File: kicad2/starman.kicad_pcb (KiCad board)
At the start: 2 copper layers, 160 x 150 mm, 156 parts, among them J1 Barrel_Jack, P1 USB_C_Plug_USB2.0, U1 ESP32-S2-MINI-1, U2 PCA9959, U3 PCA9959, U4 PCA9959, U5 PCA9959, U6 LF33_TO220, U7 LF50_TO220, U8 PCA9959, U9 PCA9959

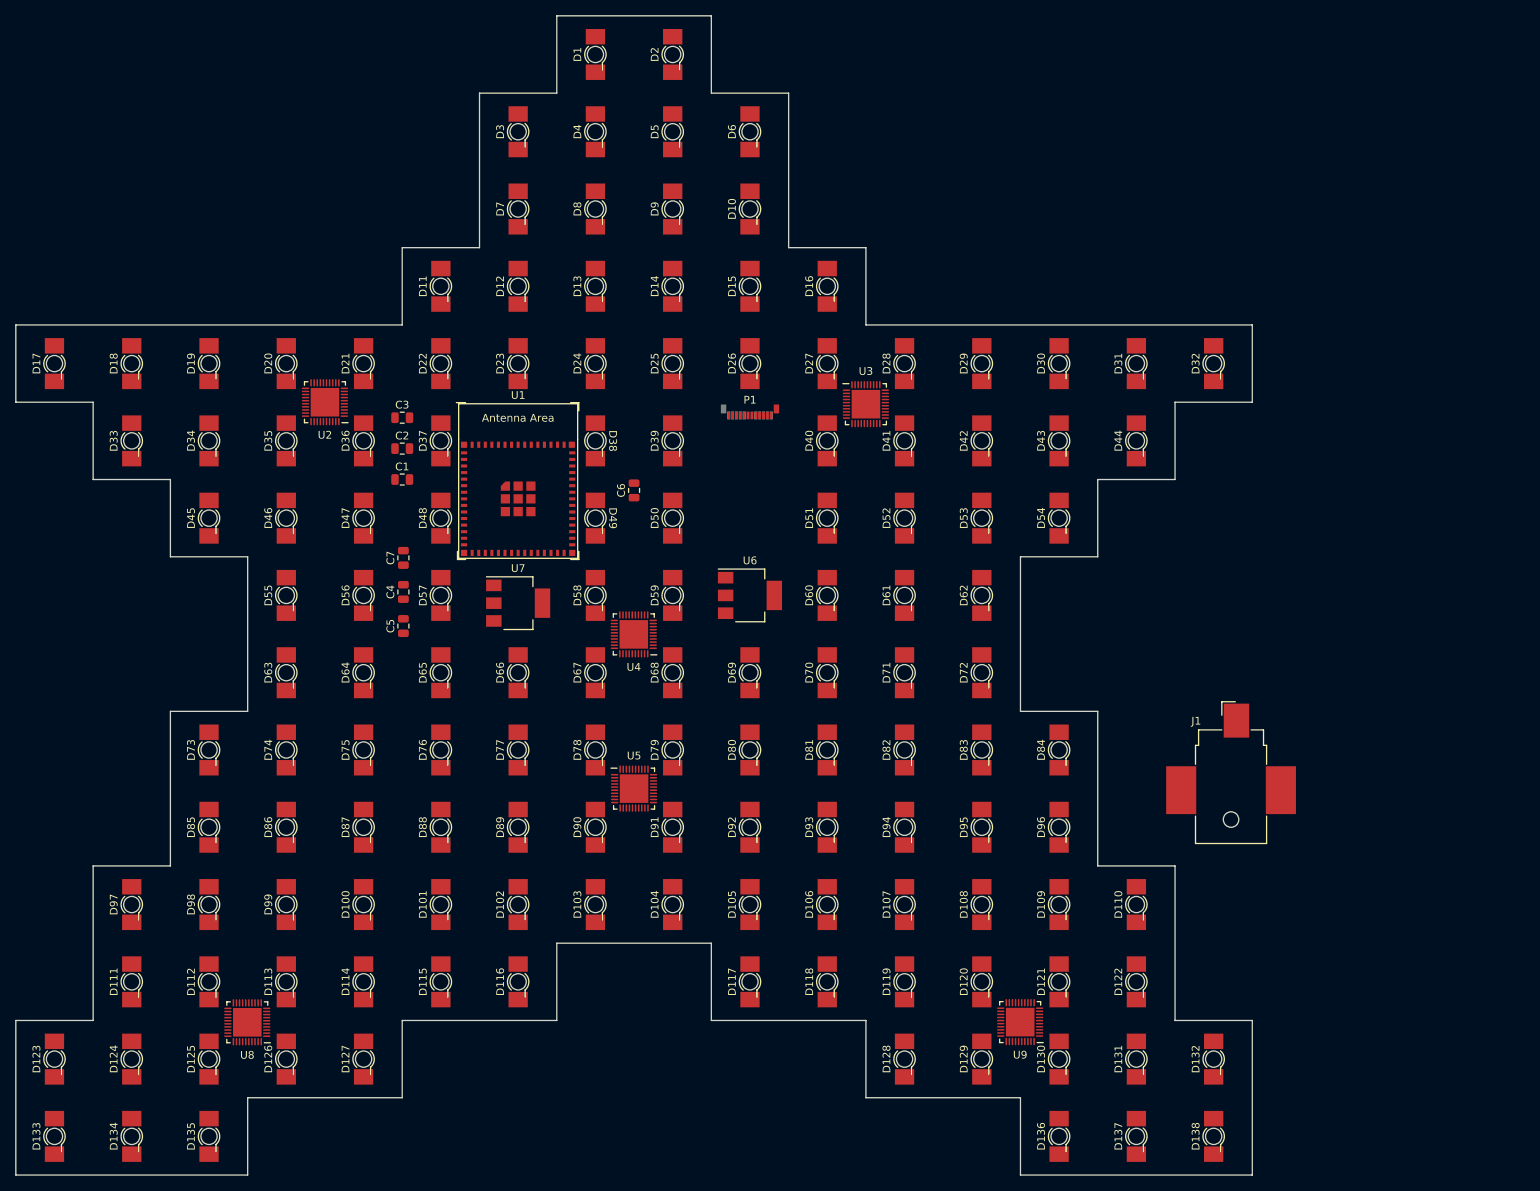
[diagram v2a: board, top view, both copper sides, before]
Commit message: Route U2 and U3 LEDs
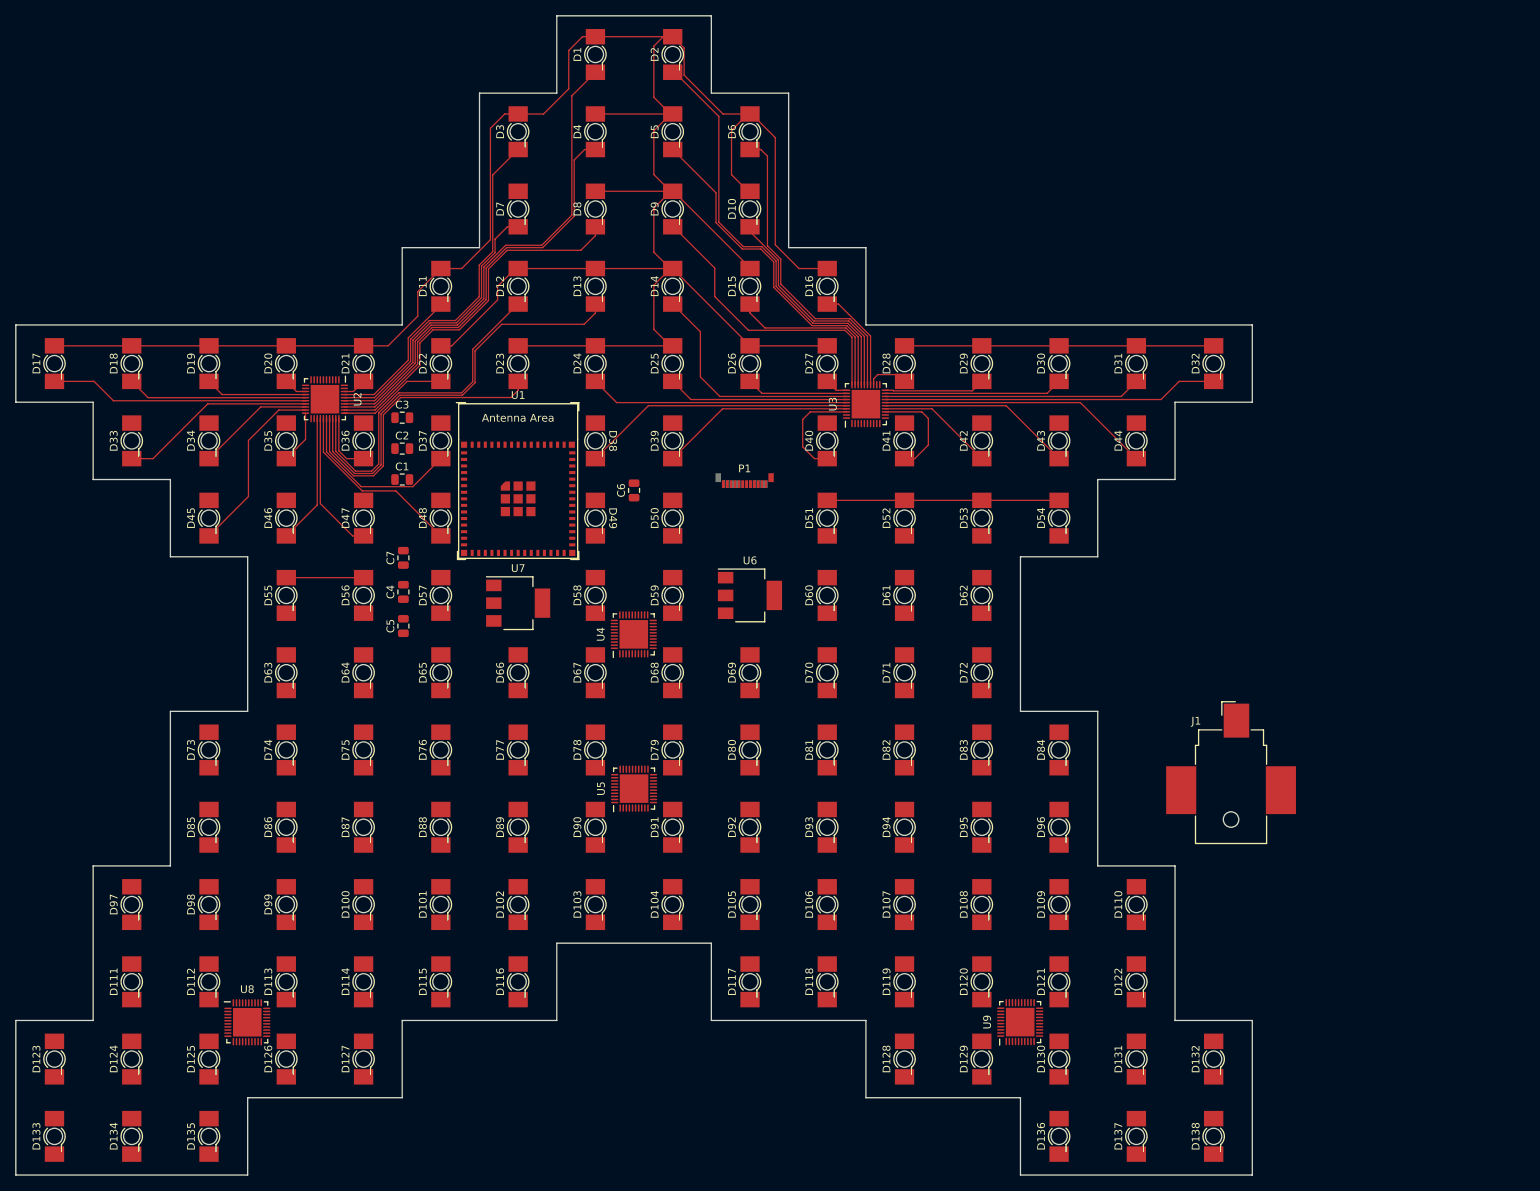
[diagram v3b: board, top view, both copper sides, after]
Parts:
- moved P1 8.92 mm to (124.3, 90.6)
- moved U2 0.39 mm to (70.0, 79.6), turned to 270 degrees
- turned U3 to 90 degrees
- turned U4 to 90 degrees
- turned U5 to 90 degrees
- turned U8 to 0 degrees
- turned U9 to 90 degrees
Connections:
- D1 pad 2: Net-(D1-Pad2) -> (no net)
- D10 pad 2: Net-(D10-Pad2) -> (no net)
- D100 pad 2: Net-(D100-Pad2) -> (no net)
- D101 pad 2: Net-(D101-Pad2) -> (no net)
- D102 pad 2: Net-(D102-Pad2) -> (no net)
- D103 pad 2: Net-(D103-Pad2) -> (no net)
- D104 pad 2: Net-(D104-Pad2) -> (no net)
- D105 pad 2: Net-(D105-Pad2) -> (no net)
- D106 pad 2: Net-(D106-Pad2) -> (no net)
- D107 pad 2: Net-(D107-Pad2) -> (no net)
- D108 pad 2: Net-(D108-Pad2) -> (no net)
- D109 pad 2: Net-(D109-Pad2) -> (no net)
- D11 pad 2: Net-(D11-Pad2) -> (no net)
- D110 pad 2: Net-(D110-Pad2) -> (no net)
- D111 pad 2: Net-(D111-Pad2) -> (no net)
- D112 pad 2: Net-(D112-Pad2) -> (no net)
- D113 pad 2: Net-(D113-Pad2) -> (no net)
- D114 pad 2: Net-(D114-Pad2) -> (no net)
- D115 pad 2: Net-(D115-Pad2) -> (no net)
- D116 pad 2: Net-(D116-Pad2) -> (no net)
- D117 pad 2: Net-(D117-Pad2) -> (no net)
- D118 pad 2: Net-(D118-Pad2) -> (no net)
- D119 pad 2: Net-(D119-Pad2) -> (no net)
- D12 pad 2: Net-(D12-Pad2) -> (no net)
- D120 pad 2: Net-(D120-Pad2) -> (no net)
- D121 pad 2: Net-(D121-Pad2) -> (no net)
- D122 pad 2: Net-(D122-Pad2) -> (no net)
- D123 pad 2: Net-(D123-Pad2) -> (no net)
- D124 pad 2: Net-(D124-Pad2) -> (no net)
- D125 pad 2: Net-(D125-Pad2) -> (no net)
- D126 pad 2: Net-(D126-Pad2) -> (no net)
- D127 pad 2: Net-(D127-Pad2) -> (no net)
- D128 pad 2: Net-(D128-Pad2) -> (no net)
- D129 pad 2: Net-(D129-Pad2) -> (no net)
- D13 pad 2: Net-(D13-Pad2) -> (no net)
- D130 pad 2: Net-(D130-Pad2) -> (no net)
- D131 pad 2: Net-(D131-Pad2) -> (no net)
- D132 pad 2: Net-(D132-Pad2) -> (no net)
- D133 pad 2: Net-(D133-Pad2) -> (no net)
- D134 pad 2: Net-(D134-Pad2) -> (no net)
- D135 pad 2: Net-(D135-Pad2) -> (no net)
- D136 pad 2: Net-(D136-Pad2) -> (no net)
- D137 pad 2: Net-(D137-Pad2) -> (no net)
- D138 pad 2: Net-(D138-Pad2) -> (no net)
- D14 pad 2: Net-(D14-Pad2) -> (no net)
- D15 pad 2: Net-(D15-Pad2) -> (no net)
- D16 pad 2: Net-(D16-Pad2) -> (no net)
- D17 pad 2: Net-(D17-Pad2) -> (no net)
- D18 pad 2: Net-(D18-Pad2) -> (no net)
- D19 pad 2: Net-(D19-Pad2) -> (no net)
- D2 pad 2: Net-(D2-Pad2) -> (no net)
- D20 pad 2: Net-(D20-Pad2) -> (no net)
- D21 pad 2: Net-(D21-Pad2) -> (no net)
- D22 pad 2: Net-(D22-Pad2) -> (no net)
- D23 pad 2: Net-(D23-Pad2) -> (no net)
- D24 pad 2: Net-(D24-Pad2) -> (no net)
- D25 pad 2: Net-(D25-Pad2) -> (no net)
- D26 pad 2: Net-(D26-Pad2) -> (no net)
- D27 pad 2: Net-(D27-Pad2) -> (no net)
- D28 pad 2: Net-(D28-Pad2) -> (no net)
- D29 pad 2: Net-(D29-Pad2) -> (no net)
- D3 pad 2: Net-(D3-Pad2) -> (no net)
- D30 pad 2: Net-(D30-Pad2) -> (no net)
- D31 pad 2: Net-(D31-Pad2) -> (no net)
- D32 pad 2: Net-(D32-Pad2) -> (no net)
- D33 pad 2: Net-(D33-Pad2) -> (no net)
- D34 pad 2: Net-(D34-Pad2) -> (no net)
- D35 pad 2: Net-(D35-Pad2) -> (no net)
- D36 pad 2: Net-(D36-Pad2) -> (no net)
- D37 pad 2: Net-(D37-Pad2) -> (no net)
- D38 pad 2: Net-(D38-Pad2) -> (no net)
- D39 pad 2: Net-(D39-Pad2) -> (no net)
- D4 pad 2: Net-(D4-Pad2) -> (no net)
- D40 pad 2: Net-(D40-Pad2) -> (no net)
- D41 pad 2: Net-(D41-Pad2) -> (no net)
- D42 pad 2: Net-(D42-Pad2) -> (no net)
- D43 pad 2: Net-(D43-Pad2) -> (no net)
- D44 pad 2: Net-(D44-Pad2) -> (no net)
- D45 pad 2: Net-(D45-Pad2) -> (no net)
- D46 pad 2: Net-(D46-Pad2) -> (no net)
- D47 pad 2: Net-(D47-Pad2) -> (no net)
- D48 pad 2: Net-(D48-Pad2) -> (no net)
- D49 pad 2: Net-(D49-Pad2) -> (no net)
- D5 pad 2: Net-(D5-Pad2) -> (no net)
- D50 pad 2: Net-(D50-Pad2) -> (no net)
- D51 pad 2: Net-(D51-Pad2) -> (no net)
- D52 pad 2: Net-(D52-Pad2) -> (no net)
- D53 pad 2: Net-(D53-Pad2) -> (no net)
- D54 pad 2: Net-(D54-Pad2) -> (no net)
- D55 pad 2: Net-(D55-Pad2) -> (no net)
- D56 pad 2: Net-(D56-Pad2) -> (no net)
- D57 pad 2: Net-(D57-Pad2) -> (no net)
- D58 pad 2: Net-(D58-Pad2) -> (no net)
- D59 pad 2: Net-(D59-Pad2) -> (no net)
- D6 pad 2: Net-(D6-Pad2) -> (no net)
- D60 pad 2: Net-(D60-Pad2) -> (no net)
- D61 pad 2: Net-(D61-Pad2) -> (no net)
- D62 pad 2: Net-(D62-Pad2) -> (no net)
- D63 pad 2: Net-(D63-Pad2) -> (no net)
- D64 pad 2: Net-(D64-Pad2) -> (no net)
- D65 pad 2: Net-(D65-Pad2) -> (no net)
- D66 pad 2: Net-(D66-Pad2) -> (no net)
- D67 pad 2: Net-(D67-Pad2) -> (no net)
- D68 pad 2: Net-(D68-Pad2) -> (no net)
- D69 pad 2: Net-(D69-Pad2) -> (no net)
- D7 pad 2: Net-(D7-Pad2) -> (no net)
- D70 pad 2: Net-(D70-Pad2) -> (no net)
- D71 pad 2: Net-(D71-Pad2) -> (no net)
- D72 pad 2: Net-(D72-Pad2) -> (no net)
- D73 pad 1: Net-(D73-Pad1) -> (no net)
- D73 pad 2: Net-(D73-Pad2) -> (no net)
- D74 pad 2: Net-(D74-Pad2) -> (no net)
- D75 pad 2: Net-(D75-Pad2) -> (no net)
- D76 pad 2: Net-(D76-Pad2) -> (no net)
- D77 pad 2: Net-(D77-Pad2) -> (no net)
- D78 pad 2: Net-(D78-Pad2) -> (no net)
- D79 pad 2: Net-(D79-Pad2) -> (no net)
- D8 pad 2: Net-(D8-Pad2) -> (no net)
- D80 pad 2: Net-(D80-Pad2) -> (no net)
- D81 pad 2: Net-(D81-Pad2) -> (no net)
- D82 pad 2: Net-(D82-Pad2) -> (no net)
- D83 pad 2: Net-(D83-Pad2) -> (no net)
- D84 pad 2: Net-(D84-Pad2) -> (no net)
- D85 pad 2: Net-(D85-Pad2) -> (no net)
- D86 pad 2: Net-(D86-Pad2) -> (no net)
- D87 pad 2: Net-(D87-Pad2) -> (no net)
- D88 pad 2: Net-(D88-Pad2) -> (no net)
- D89 pad 2: Net-(D89-Pad2) -> (no net)
- D9 pad 2: Net-(D9-Pad2) -> (no net)
- D90 pad 2: Net-(D90-Pad2) -> (no net)
- D91 pad 2: Net-(D91-Pad2) -> (no net)
- D92 pad 2: Net-(D92-Pad2) -> (no net)
- D93 pad 2: Net-(D93-Pad2) -> (no net)
- D94 pad 2: Net-(D94-Pad2) -> (no net)
- D95 pad 2: Net-(D95-Pad2) -> (no net)
- D96 pad 2: Net-(D96-Pad2) -> (no net)
- D97 pad 2: Net-(D97-Pad2) -> (no net)
- D98 pad 2: Net-(D98-Pad2) -> (no net)
- D99 pad 2: Net-(D99-Pad2) -> (no net)
- P1 pad A5: Net-(P1-PadA5) -> (no net)
- P1 pad A8: Net-(P1-PadA8) -> (no net)
- P1 pad B5: Net-(P1-PadB5) -> (no net)
- P1 pad B8: Net-(P1-PadB8) -> (no net)
- U1 pad 10: Net-(U1-Pad10) -> (no net)
- U1 pad 11: Net-(U1-Pad11) -> (no net)
- U1 pad 12: Net-(U1-Pad12) -> (no net)
- U1 pad 13: Net-(U1-Pad13) -> (no net)
- U1 pad 14: Net-(U1-Pad14) -> (no net)
- U1 pad 15: Net-(U1-Pad15) -> (no net)
- U1 pad 16: Net-(U1-Pad16) -> (no net)
- U1 pad 17: Net-(U1-Pad17) -> (no net)
- U1 pad 18: Net-(U1-Pad18) -> (no net)
- U1 pad 19: Net-(U1-Pad19) -> (no net)
- U1 pad 20: Net-(U1-Pad20) -> (no net)
- U1 pad 21: Net-(U1-Pad21) -> (no net)
- U1 pad 22: Net-(U1-Pad22) -> (no net)
- U1 pad 25: Net-(U1-Pad25) -> (no net)
- U1 pad 26: Net-(U1-Pad26) -> (no net)
- U1 pad 27: Net-(U1-Pad27) -> (no net)
- U1 pad 28: Net-(U1-Pad28) -> (no net)
- U1 pad 29: Net-(U1-Pad29) -> (no net)
- U1 pad 31: Net-(U1-Pad31) -> (no net)
- U1 pad 32: Net-(U1-Pad32) -> (no net)
- U1 pad 33: Net-(U1-Pad33) -> (no net)
- U1 pad 34: Net-(U1-Pad34) -> (no net)
- U1 pad 35: Net-(U1-Pad35) -> (no net)
- U1 pad 36: Net-(U1-Pad36) -> (no net)
- U1 pad 37: Net-(U1-Pad37) -> (no net)
- U1 pad 38: Net-(U1-Pad38) -> (no net)
- U1 pad 39: Net-(U1-Pad39) -> (no net)
- U1 pad 4: /BOOT -> (no net)
- U1 pad 40: Net-(U1-Pad40) -> (no net)
- U1 pad 41: Net-(U1-Pad41) -> (no net)
- U1 pad 44: Net-(U1-Pad44) -> (no net)
- U1 pad 45: /RESET -> (no net)
- U1 pad 5: /IREF -> (no net)
- U1 pad 6: /BLANK -> (no net)
- U1 pad 7: /XLAT -> (no net)
- U1 pad 8: /SCLK -> (no net)
- U1 pad 9: /SIN -> (no net)
- U2 pad 1: Net-(U2-Pad1) -> (no net)
- U2 pad 10: Net-(U2-Pad10) -> (no net)
- U2 pad 11: Net-(U2-Pad11) -> (no net)
- U2 pad 12: Net-(U2-Pad12) -> (no net)
- U2 pad 13: Net-(D1-Pad1) -> Net-(D20-Pad1)
- U2 pad 14: Net-(D3-Pad1) -> Net-(D19-Pad1)
- U2 pad 15: Net-(D4-Pad1) -> Net-(D18-Pad1)
- U2 pad 16: Net-(D7-Pad1) -> Net-(D17-Pad1)
- U2 pad 17: Net-(D8-Pad1) -> Net-(D33-Pad1)
- U2 pad 18: Net-(D11-Pad1) -> Net-(D34-Pad1)
- U2 pad 19: Net-(D12-Pad1) -> Net-(D45-Pad1)
- U2 pad 2: Net-(U2-Pad2) -> (no net)
- U2 pad 20: Net-(D13-Pad1) -> Net-(D35-Pad1)
- U2 pad 21: Net-(U2-Pad21) -> (no net)
- U2 pad 22: Net-(U2-Pad22) -> (no net)
- U2 pad 23: Net-(D17-Pad1) -> Net-(D46-Pad1)
- U2 pad 24: Net-(D18-Pad1) -> Net-(D47-Pad1)
- U2 pad 25: Net-(D19-Pad1) -> Net-(D48-Pad1)
- U2 pad 26: Net-(D20-Pad1) -> Net-(D37-Pad1)
- U2 pad 27: Net-(D21-Pad1) -> Net-(D23-Pad1)
- U2 pad 28: Net-(D22-Pad1) -> Net-(D13-Pad1)
- U2 pad 29: Net-(D23-Pad1) -> Net-(D12-Pad1)
- U2 pad 3: Net-(U2-Pad3) -> (no net)
- U2 pad 30: Net-(D33-Pad1) -> Net-(D36-Pad1)
- U2 pad 31: Net-(D34-Pad1) -> Net-(D22-Pad1)
- U2 pad 32: Net-(D35-Pad1) -> Net-(D8-Pad1)
- U2 pad 33: Net-(D36-Pad1) -> Net-(D4-Pad1)
- U2 pad 34: Net-(D37-Pad1) -> Net-(D1-Pad1)
- U2 pad 35: Net-(D45-Pad1) -> Net-(D7-Pad1)
- U2 pad 36: Net-(D46-Pad1) -> Net-(D3-Pad1)
- U2 pad 37: Net-(D47-Pad1) -> Net-(D11-Pad1)
- U2 pad 38: Net-(D48-Pad1) -> Net-(D21-Pad1)
- U2 pad 39: Net-(U2-Pad39) -> (no net)
- U2 pad 4: Net-(U2-Pad4) -> (no net)
- U2 pad 40: Net-(U2-Pad40) -> (no net)
- U2 pad 5: Net-(U2-Pad5) -> (no net)
- U2 pad 6: Net-(U2-Pad6) -> (no net)
- U2 pad 7: Net-(U2-Pad7) -> (no net)
- U2 pad 8: Net-(U2-Pad8) -> (no net)
- U2 pad 9: Net-(U2-Pad9) -> (no net)
- U3 pad 1: Net-(U3-Pad1) -> (no net)
- U3 pad 10: Net-(U3-Pad10) -> (no net)
- U3 pad 11: Net-(U3-Pad11) -> (no net)
- U3 pad 12: Net-(U3-Pad12) -> (no net)
- U3 pad 13: Net-(D2-Pad1) -> Net-(D41-Pad1)
- U3 pad 14: Net-(D5-Pad1) -> Net-(D42-Pad1)
- U3 pad 15: Net-(D6-Pad1) -> Net-(D43-Pad1)
- U3 pad 16: Net-(D9-Pad1) -> Net-(D44-Pad1)
- U3 pad 17: Net-(D10-Pad1) -> Net-(D32-Pad1)
- U3 pad 18: Net-(D14-Pad1) -> Net-(D31-Pad1)
- U3 pad 19: Net-(D15-Pad1) -> Net-(D30-Pad1)
- U3 pad 2: Net-(U3-Pad2) -> (no net)
- U3 pad 20: Net-(D16-Pad1) -> Net-(D29-Pad1)
- U3 pad 21: Net-(U3-Pad21) -> (no net)
- U3 pad 22: Net-(U3-Pad22) -> (no net)
- U3 pad 23: Net-(D24-Pad1) -> Net-(D28-Pad1)
- U3 pad 24: Net-(D25-Pad1) -> Net-(D16-Pad1)
- U3 pad 25: Net-(D26-Pad1) -> Net-(D6-Pad1)
- U3 pad 26: Net-(D27-Pad1) -> Net-(D10-Pad1)
- U3 pad 27: Net-(D28-Pad1) -> Net-(D2-Pad1)
- U3 pad 28: Net-(D29-Pad1) -> Net-(D5-Pad1)
- U3 pad 29: Net-(D30-Pad1) -> Net-(D15-Pad1)
- U3 pad 3: Net-(U3-Pad3) -> (no net)
- U3 pad 30: Net-(D31-Pad1) -> Net-(D9-Pad1)
- U3 pad 31: Net-(D32-Pad1) -> Net-(D27-Pad1)
- U3 pad 32: Net-(D38-Pad1) -> Net-(D26-Pad1)
- U3 pad 33: Net-(D39-Pad1) -> Net-(D14-Pad1)
- U3 pad 34: Net-(D40-Pad1) -> Net-(D25-Pad1)
- U3 pad 35: Net-(D41-Pad1) -> Net-(D24-Pad1)
- U3 pad 36: Net-(D42-Pad1) -> Net-(D38-Pad1)
- U3 pad 37: Net-(D43-Pad1) -> Net-(D39-Pad1)
- U3 pad 38: Net-(D44-Pad1) -> Net-(D40-Pad1)
- U3 pad 39: Net-(U3-Pad39) -> (no net)
- U3 pad 4: Net-(U3-Pad4) -> (no net)
- U3 pad 40: Net-(U3-Pad40) -> (no net)
- U3 pad 5: Net-(U3-Pad5) -> (no net)
- U3 pad 6: Net-(U3-Pad6) -> (no net)
- U3 pad 7: Net-(U3-Pad7) -> (no net)
- U3 pad 8: Net-(U3-Pad8) -> (no net)
- U3 pad 9: Net-(U3-Pad9) -> (no net)
- U4 pad 1: Net-(U4-Pad1) -> (no net)
- U4 pad 10: Net-(U4-Pad10) -> (no net)
- U4 pad 11: Net-(U4-Pad11) -> (no net)
- U4 pad 12: Net-(U4-Pad12) -> (no net)
- U4 pad 2: Net-(U4-Pad2) -> (no net)
- U4 pad 21: Net-(U4-Pad21) -> (no net)
- U4 pad 22: Net-(U4-Pad22) -> (no net)
- U4 pad 3: Net-(U4-Pad3) -> (no net)
- U4 pad 39: Net-(U4-Pad39) -> (no net)
- U4 pad 4: Net-(U4-Pad4) -> (no net)
- U4 pad 40: Net-(U4-Pad40) -> (no net)
- U4 pad 5: Net-(U4-Pad5) -> (no net)
- U4 pad 6: Net-(U4-Pad6) -> (no net)
- U4 pad 7: Net-(U4-Pad7) -> (no net)
- U4 pad 8: Net-(U4-Pad8) -> (no net)
- U4 pad 9: Net-(U4-Pad9) -> (no net)
- U5 pad 1: Net-(U5-Pad1) -> (no net)
- U5 pad 10: Net-(U5-Pad10) -> (no net)
- U5 pad 11: Net-(U5-Pad11) -> (no net)
- U5 pad 12: Net-(U5-Pad12) -> (no net)
- U5 pad 13: Net-(D73-Pad1) -> (no net)
- U5 pad 14: Net-(D74-Pad1) -> Net-(D96-Pad1)
- U5 pad 15: Net-(D75-Pad1) -> Net-(D95-Pad1)
- U5 pad 16: Net-(D76-Pad1) -> Net-(D94-Pad1)
- U5 pad 17: Net-(D77-Pad1) -> Net-(D93-Pad1)
- U5 pad 18: Net-(D78-Pad1) -> Net-(D92-Pad1)
- U5 pad 19: Net-(D79-Pad1) -> Net-(D91-Pad1)
- U5 pad 2: Net-(U5-Pad2) -> (no net)
- U5 pad 20: Net-(D80-Pad1) -> Net-(D90-Pad1)
- U5 pad 21: Net-(U5-Pad21) -> (no net)
- U5 pad 22: Net-(U5-Pad22) -> (no net)
- U5 pad 23: Net-(D81-Pad1) -> Net-(D89-Pad1)
- U5 pad 24: Net-(D82-Pad1) -> Net-(D88-Pad1)
- U5 pad 25: Net-(D83-Pad1) -> Net-(D87-Pad1)
- U5 pad 26: Net-(D84-Pad1) -> Net-(D86-Pad1)
- U5 pad 28: Net-(D86-Pad1) -> Net-(D84-Pad1)
- U5 pad 29: Net-(D87-Pad1) -> Net-(D83-Pad1)
- U5 pad 3: Net-(U5-Pad3) -> (no net)
- U5 pad 30: Net-(D88-Pad1) -> Net-(D82-Pad1)
- U5 pad 31: Net-(D89-Pad1) -> Net-(D81-Pad1)
- U5 pad 32: Net-(D90-Pad1) -> Net-(D80-Pad1)
- U5 pad 33: Net-(D91-Pad1) -> Net-(D79-Pad1)
- U5 pad 34: Net-(D92-Pad1) -> Net-(D78-Pad1)
- U5 pad 35: Net-(D93-Pad1) -> Net-(D77-Pad1)
- U5 pad 36: Net-(D94-Pad1) -> Net-(D76-Pad1)
- U5 pad 37: Net-(D95-Pad1) -> Net-(D75-Pad1)
- U5 pad 38: Net-(D96-Pad1) -> Net-(D74-Pad1)
- U5 pad 39: Net-(U5-Pad39) -> (no net)
- U5 pad 4: Net-(U5-Pad4) -> (no net)
- U5 pad 40: Net-(U5-Pad40) -> (no net)
- U5 pad 5: Net-(U5-Pad5) -> (no net)
- U5 pad 6: Net-(U5-Pad6) -> (no net)
- U5 pad 7: Net-(U5-Pad7) -> (no net)
- U5 pad 8: Net-(U5-Pad8) -> (no net)
- U5 pad 9: Net-(U5-Pad9) -> (no net)
- U8 pad 1: Net-(U8-Pad1) -> (no net)
- U8 pad 10: Net-(U8-Pad10) -> (no net)
- U8 pad 11: Net-(U8-Pad11) -> (no net)
- U8 pad 12: Net-(U8-Pad12) -> (no net)
- U8 pad 2: Net-(U8-Pad2) -> (no net)
- U8 pad 21: Net-(U8-Pad21) -> (no net)
- U8 pad 22: Net-(U8-Pad22) -> (no net)
- U8 pad 3: Net-(U8-Pad3) -> (no net)
- U8 pad 36: Net-(U8-Pad36) -> (no net)
- U8 pad 37: Net-(U8-Pad37) -> (no net)
- U8 pad 38: Net-(U8-Pad38) -> (no net)
- U8 pad 39: Net-(U8-Pad39) -> (no net)
- U8 pad 4: Net-(U8-Pad4) -> (no net)
- U8 pad 40: Net-(U8-Pad40) -> (no net)
- U8 pad 5: Net-(U8-Pad5) -> (no net)
- U8 pad 6: Net-(U8-Pad6) -> (no net)
- U8 pad 7: Net-(U8-Pad7) -> (no net)
- U8 pad 8: Net-(U8-Pad8) -> (no net)
- U8 pad 9: Net-(U8-Pad9) -> (no net)
- U9 pad 1: Net-(U9-Pad1) -> (no net)
- U9 pad 10: Net-(U9-Pad10) -> (no net)
- U9 pad 11: Net-(U9-Pad11) -> (no net)
- U9 pad 12: Net-(U9-Pad12) -> (no net)
- U9 pad 2: Net-(U9-Pad2) -> (no net)
- U9 pad 21: Net-(U9-Pad21) -> (no net)
- U9 pad 22: Net-(U9-Pad22) -> (no net)
- U9 pad 3: Net-(U9-Pad3) -> (no net)
- U9 pad 36: Net-(U9-Pad36) -> (no net)
- U9 pad 37: Net-(U9-Pad37) -> (no net)
- U9 pad 38: Net-(U9-Pad38) -> (no net)
- U9 pad 39: Net-(U9-Pad39) -> (no net)
- U9 pad 4: Net-(U9-Pad4) -> (no net)
- U9 pad 40: Net-(U9-Pad40) -> (no net)
- U9 pad 5: Net-(U9-Pad5) -> (no net)
- U9 pad 6: Net-(U9-Pad6) -> (no net)
- U9 pad 7: Net-(U9-Pad7) -> (no net)
- U9 pad 8: Net-(U9-Pad8) -> (no net)
- U9 pad 9: Net-(U9-Pad9) -> (no net)
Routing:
- net (no net): track 0.00 -> 408.1 mm
- net Net-(D1-Pad1): track 0.00 -> 63.4 mm
- net Net-(D13-Pad1): track 0.00 -> 55.5 mm
- net Net-(D2-Pad1): track 0.00 -> 54.7 mm
- net Net-(D4-Pad1): track 0.00 -> 54.6 mm
- net Net-(D8-Pad1): track 0.00 -> 47.1 mm
- net Net-(D3-Pad1): track 0.00 -> 45.7 mm
- net Net-(D5-Pad1): track 0.00 -> 44.4 mm
- net Net-(D12-Pad1): track 0.00 -> 44.2 mm
- net Net-(D32-Pad1): track 0.00 -> 43.5 mm
- net Net-(D6-Pad1): track 0.00 -> 40.2 mm
- net Net-(D23-Pad1): track 0.00 -> 39.6 mm
- net Net-(D9-Pad1): track 0.00 -> 37.4 mm
- net Net-(D7-Pad1): track 0.00 -> 36.9 mm
- net Net-(D44-Pad1): track 0.00 -> 35.5 mm
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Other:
- net class Default: clearance 0.2 -> 0.15; trace_width 0.25 -> 0.15
- rule trace_clearance: 0.2 -> 0.15
- rule trace_min: 0.2 -> 0.15
